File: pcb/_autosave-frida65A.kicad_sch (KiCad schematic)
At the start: 68 parts, among them J1 TP_PWR, J10 TP_LOGIC, J11 TP_OUT, J12 J_P, J16 J_N, J17 Molex_02x04_Mini-Fit_Jr, J2 CONN_IN_P, J3 CONN_IN_N, J4 TP_CFG, J5 CONN_CFG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

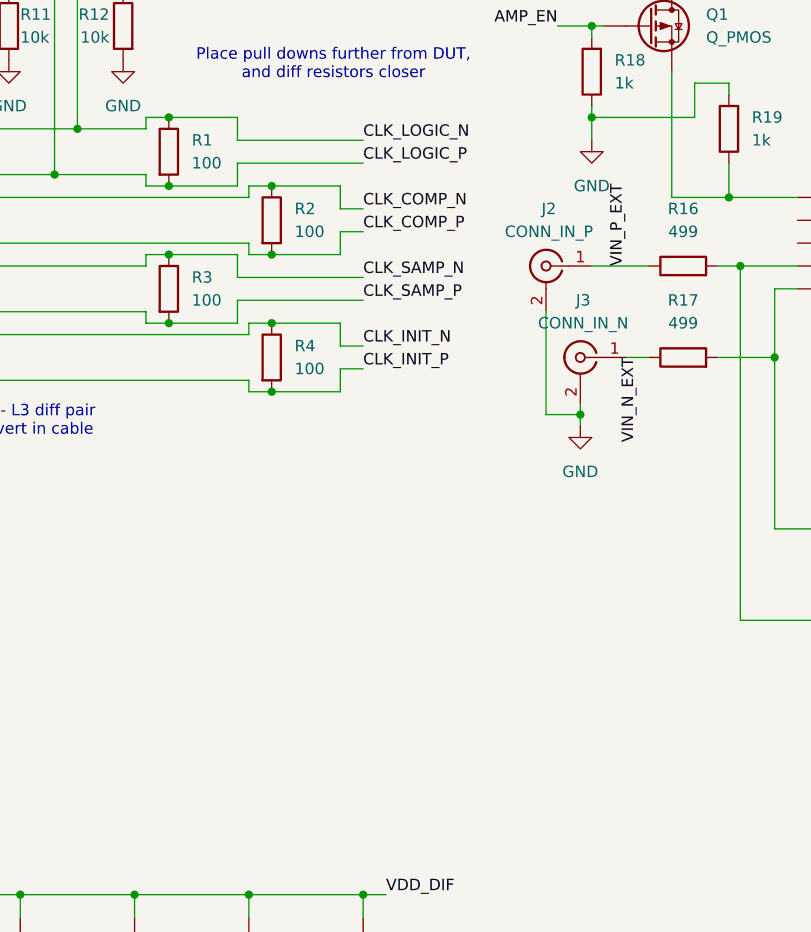
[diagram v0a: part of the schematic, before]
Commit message: schematic of daq hdl
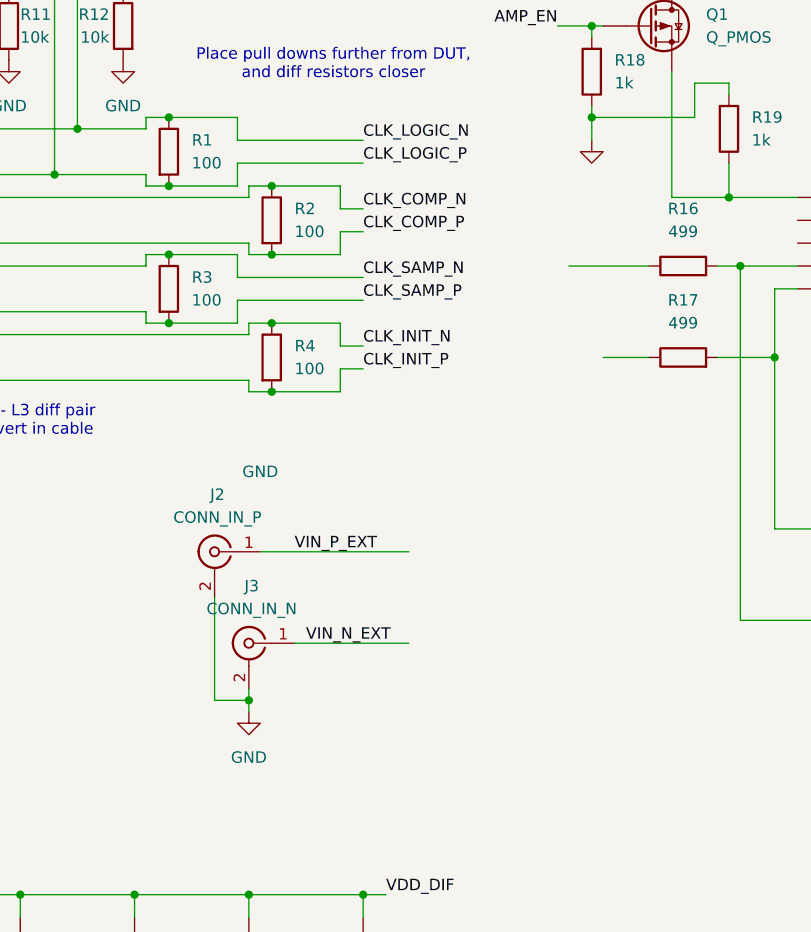
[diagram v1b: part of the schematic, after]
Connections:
- net VIN_N_EXT: no longer R17.1
- net VIN_P_EXT: no longer R16.1
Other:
- moved on the sheet: J2, J3
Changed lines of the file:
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@@
 	)
 	(junction
-		(at 152.4 72.39)
+		(at 115.57 104.14)
 		(diameter 0)
 		(color 0 0 0 0)
@@
 	(wire
 		(pts
-			(xy 152.4 72.39) (xy 152.4 73.66)
+			(xy 115.57 104.14) (xy 115.57 105.41)
 		)
 		(stroke
@@
 	(wire
 		(pts
+			(xy 154.94 66.04) (xy 160.02 66.04)
+		)
+		(stroke
+			(width 0)
+			(type default)
+		)
+	)
+	(wire
+		(pts
 			(xy 31.75 71.12) (xy 48.26 71.12)
 		)
@@
 	(wire
 		(pts
-			(xy 152.4 71.12) (xy 152.4 72.39)
+			(xy 115.57 102.87) (xy 115.57 104.14)
 		)
 		(stroke
@@
 	(wire
 		(pts
-			(xy 157.48 66.04) (xy 160.02 66.04)
+			(xy 120.65 97.79) (xy 133.35 97.79)
 		)
 		(stroke
@@
 	(wire
 		(pts
-			(xy 148.59 72.39) (xy 152.4 72.39)
+			(xy 111.76 104.14) (xy 115.57 104.14)
 		)
 		(stroke
@@
 	(wire
 		(pts
-			(xy 153.67 55.88) (xy 160.02 55.88)
+			(xy 116.84 87.63) (xy 133.35 87.63)
 		)
 		(stroke
@@
 	(wire
 		(pts
-			(xy 148.59 60.96) (xy 148.59 72.39)
+			(xy 111.76 92.71) (xy 111.76 104.14)
 		)
 		(stroke
@@
 	(wire
 		(pts
+			(xy 151.13 55.88) (xy 160.02 55.88)
+		)
+		(stroke
+			(width 0)
+			(type default)
+		)
+	)
+	(wire
+		(pts
 			(xy 54.61 128.27) (xy 54.61 176.53)
 		)
@@
 	)
 	(label "VIN_N_EXT"
-		(at 158.75 66.04 270)
+		(at 121.92 97.79 0)
 		(effects
 			(font
 				(size 1.27 1.27)
 			)
-			(justify right bottom)
+			(justify left bottom)
 		)
 	)
@@
 	)
 	(label "VIN_P_EXT"
-		(at 157.48 55.88 90)
+		(at 120.65 87.63 0)
 		(effects
 			(font
@@
 	(symbol
 		(lib_id "dmaps_components:Conn_LEMO")
-		(at 152.4 66.04 0)
+		(at 115.57 97.79 0)
 		(unit 1)
 		(exclude_from_sim no)
@@
 		(fields_autoplaced yes)
 		(property "Reference" "J3"
-			(at 152.7175 59.69 0)
+			(at 115.8875 91.44 0)
 			(effects
 				(font
@@
 		)
 		(property "Value" "CONN_IN_N"
-			(at 152.7175 62.23 0)
+			(at 115.8875 93.98 0)
 			(effects
 				(font
@@
 		)
 		(property "Footprint" "Connector_Coaxial:SMA_Amphenol_901-143_Horizontal"
-			(at 152.4 66.04 0)
+			(at 115.57 97.79 0)
 			(effects
 				(font
@@
 		)
 		(property "Datasheet" "~"
-			(at 152.4 66.04 0)
+			(at 115.57 97.79 0)
 			(effects
 				(font
@@
 		)
 		(property "Description" "coaxial connector (BNC, SMA, SMB, SMC, Cinch/RCA, ...)"
-			(at 152.4 66.04 0)
+			(at 115.57 97.79 0)
 			(effects
 				(font
@@
 	(symbol
 		(lib_id "dmaps_components:Conn_LEMO")
-		(at 148.59 55.88 0)
+		(at 111.76 87.63 0)
 		(unit 1)
 		(exclude_from_sim no)
@@
 		(fields_autoplaced yes)
 		(property "Reference" "J2"
-			(at 148.9075 49.53 0)
+			(at 112.0775 81.28 0)
 			(effects
 				(font
@@
 		)
 		(property "Value" "CONN_IN_P"
-			(at 148.9075 52.07 0)
+			(at 112.0775 83.82 0)
 			(effects
 				(font
@@
 		)
 		(property "Footprint" "Connector_Coaxial:SMA_Amphenol_901-143_Horizontal"
-			(at 148.59 55.88 0)
+			(at 111.76 87.63 0)
 			(effects
 				(font
@@
 		)
 		(property "Datasheet" "~"
-			(at 148.59 55.88 0)
+			(at 111.76 87.63 0)
 			(effects
 				(font
@@
 		)
 		(property "Description" "coaxial connector (BNC, SMA, SMB, SMC, Cinch/RCA, ...)"
-			(at 148.59 55.88 0)
+			(at 111.76 87.63 0)
 			(effects
 				(font
@@
 	(symbol
 		(lib_id "power:GND")
-		(at 152.4 73.66 0)
+		(at 115.57 105.41 0)
 		(mirror y)
 		(unit 1)
@@
 		(fields_autoplaced yes)
 		(property "Reference" "#PWR08"
-			(at 152.4 80.01 0)
+			(at 115.57 111.76 0)
 			(effects
 				(font
@@
 		)
 		(property "Value" "GND"
-			(at 152.4 78.74 0)
+			(at 115.57 110.49 0)
 			(effects
 				(font
@@
 		)
 		(property "Footprint" ""
-			(at 152.4 73.66 0)
+			(at 115.57 105.41 0)
 			(effects
 				(font
@@
 		)
 		(property "Datasheet" ""
-			(at 152.4 73.66 0)
+			(at 115.57 105.41 0)
 			(effects
 				(font
@@
 		)
 		(property "Description" "Power symbol creates a global label with name \"GND\" , ground"
-			(at 152.4 73.66 0)
+			(at 115.57 105.41 0)
 			(effects
 				(font
@@
 		(on_board yes)
 		(dnp no)
-		(fields_autoplaced yes)
 		(property "Reference" "#PWR07"
 			(at 153.67 48.26 0)
@@
 		)
 		(property "Value" "GND"
-			(at 153.67 46.99 0)
+			(at 116.84 78.74 0)
 			(effects
 				(font
